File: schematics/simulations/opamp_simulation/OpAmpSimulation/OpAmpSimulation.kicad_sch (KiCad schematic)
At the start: 7 parts, among them U1 ${SIM.PARAMS}

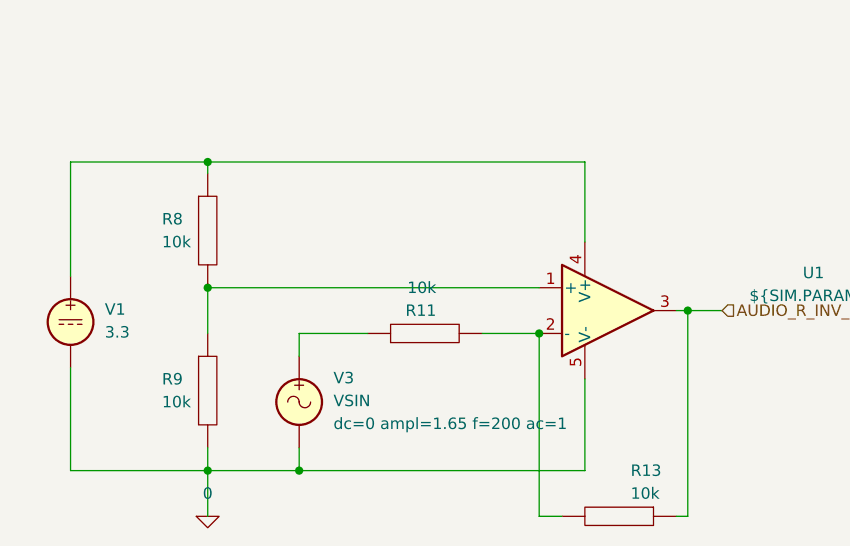
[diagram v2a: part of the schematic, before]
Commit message: [opamp_simulation:OpAmpSimulation] Ref | Replaced "R"s w/ common ones
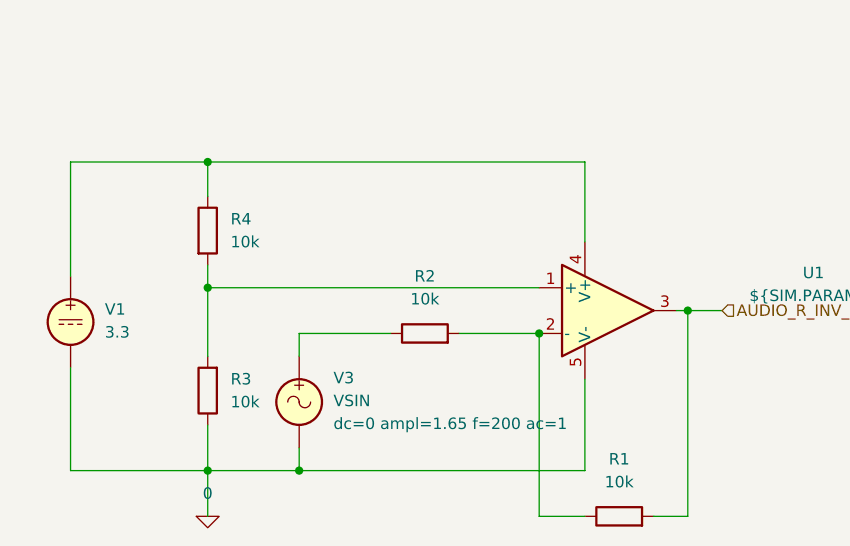
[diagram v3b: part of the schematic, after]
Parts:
- removed R11, R13, R8, R9: 10k, symbol pspice:R
- added R1, R2, R3, R4: 10k, symbol Device:R
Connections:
- net 0: now also R3.1
- net AUDIO_R_INV_SCALED: now also R1.2
- net at U1.4 (V+), V1.1: now also R4.1
- net at V3.1: now also R2.1
- net at U1.2 (-): now also R1.1, R2.2
- net at U1.1 (+): now also R3.2, R4.2
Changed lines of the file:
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@@
     (stroke (width 0) (type default))
   )
-  (wire (pts (xy 58.42 163.83) (xy 58.42 166.37))
+  (wire (pts (xy 107.95 171.45) (xy 111.76 171.45))
     (stroke (width 0) (type default))
   )
@@
     (stroke (width 0) (type default))
   )
-  (wire (pts (xy 58.42 132.08) (xy 58.42 133.35))
+  (wire (pts (xy 58.42 132.08) (xy 58.42 135.89))
     (stroke (width 0) (type default))
   )
@@
     (stroke (width 0) (type default))
   )
-  (wire (pts (xy 88.9 151.13) (xy 95.25 151.13))
-    (stroke (width 0) (type default))
-  )
   (wire (pts (xy 100.33 132.08) (xy 100.33 140.97))
     (stroke (width 0) (type default))
@@
     (stroke (width 0) (type default))
   )
-  (wire (pts (xy 68.58 151.13) (xy 76.2 151.13))
+  (wire (pts (xy 68.58 151.13) (xy 78.74 151.13))
     (stroke (width 0) (type default))
   )
@@
     (stroke (width 0) (type default))
   )
-  (wire (pts (xy 110.49 171.45) (xy 111.76 171.45))
+  (wire (pts (xy 86.36 151.13) (xy 95.25 151.13))
     (stroke (width 0) (type default))
   )
@@
     (stroke (width 0) (type default))
   )
+  (wire (pts (xy 58.42 146.05) (xy 58.42 153.67))
+    (stroke (width 0) (type default))
+  )
   (wire (pts (xy 68.58 166.37) (xy 58.42 166.37))
     (stroke (width 0) (type default))
   )
+  (wire (pts (xy 58.42 161.29) (xy 58.42 166.37))
+    (stroke (width 0) (type default))
+  )
   (wire (pts (xy 43.18 154.94) (xy 43.18 166.37))
     (stroke (width 0) (type default))
   )
-  (wire (pts (xy 58.42 146.05) (xy 58.42 151.13))
+  (wire (pts (xy 58.42 143.51) (xy 58.42 146.05))
     (stroke (width 0) (type default))
   )
@@
     (stroke (width 0) (type default))
   )
-  (wire (pts (xy 97.79 171.45) (xy 95.25 171.45))
+  (wire (pts (xy 95.25 171.45) (xy 100.33 171.45))
     (stroke (width 0) (type default))
   )
@@
     )
   )
-  (symbol (lib_id "pspice:R") (at 82.55 151.13 90) (unit 1)
-    (in_bom yes) (on_board yes) (dnp no)
-    (property "Reference" "R11" (at 83.82 148.59 90)
-      (effects (font (size 1.27 1.27)) (justify left))
-    )
-    (property "Value" "10k" (at 83.82 146.05 90)
-      (effects (font (size 1.27 1.27)) (justify left))
-    )
-    (property "Footprint" "" (at 82.55 151.13 0)
+  (symbol (lib_id "Device:R") (at 82.55 151.13 90) (unit 1)
+    (in_bom yes) (on_board yes) (dnp no) (fields_autoplaced)
+    (property "Reference" "R2" (at 82.55 144.78 90)
+      (effects (font (size 1.27 1.27)))
+    )
+    (property "Value" "10k" (at 82.55 147.32 90)
+      (effects (font (size 1.27 1.27)))
+    )
+    (property "Footprint" "" (at 82.55 152.908 90)
       (effects (font (size 1.27 1.27)) hide)
     )
@@
       (project "OpAmpSimulation"
         (path "/0d0a973c-3ed5-4fec-a6a9-6f11d3a34d9a"
-          (reference "R11") (unit 1)
-        )
-      )
-      (project "stm32f030_adc"
-        (path "/85629656-c73b-4e1f-b8e8-4366f4b01266"
-          (reference "R7") (unit 1)
-        )
-        (path "/85629656-c73b-4e1f-b8e8-4366f4b01266/b4185304-bcce-4cb1-98f3-8bffc8e76c1e"
-          (reference "R15") (unit 1)
-        )
-      )
-    )
-  )
-  (symbol (lib_id "pspice:R") (at 58.42 139.7 0) (unit 1)
-    (in_bom yes) (on_board yes) (dnp no)
-    (property "Reference" "R8" (at 53.34 138.43 0)
-      (effects (font (size 1.27 1.27)) (justify left))
-    )
-    (property "Value" "10k" (at 53.34 140.97 0)
-      (effects (font (size 1.27 1.27)) (justify left))
-    )
-    (property "Footprint" "" (at 58.42 139.7 0)
+          (reference "R2") (unit 1)
+        )
+      )
+    )
+  )
+  (symbol (lib_id "Device:R") (at 58.42 139.7 0) (unit 1)
+    (in_bom yes) (on_board yes) (dnp no) (fields_autoplaced)
+    (property "Reference" "R4" (at 60.96 138.43 0)
+      (effects (font (size 1.27 1.27)) (justify left))
+    )
+    (property "Value" "10k" (at 60.96 140.97 0)
+      (effects (font (size 1.27 1.27)) (justify left))
+    )
+    (property "Footprint" "" (at 56.642 139.7 90)
       (effects (font (size 1.27 1.27)) hide)
     )
@@
       (project "OpAmpSimulation"
         (path "/0d0a973c-3ed5-4fec-a6a9-6f11d3a34d9a"
-          (reference "R8") (unit 1)
-        )
-      )
-      (project "stm32f030_adc"
-        (path "/85629656-c73b-4e1f-b8e8-4366f4b01266"
+          (reference "R4") (unit 1)
+        )
+      )
+    )
+  )
+  (symbol (lib_id "Device:R") (at 58.42 157.48 180) (unit 1)
+    (in_bom yes) (on_board yes) (dnp no) (fields_autoplaced)
+    (property "Reference" "R3" (at 60.96 156.21 0)
+      (effects (font (size 1.27 1.27)) (justify right))
+    )
+    (property "Value" "10k" (at 60.96 158.75 0)
+      (effects (font (size 1.27 1.27)) (justify right))
+    )
+    (property "Footprint" "" (at 60.198 157.48 90)
+      (effects (font (size 1.27 1.27)) hide)
+    )
+    (property "Datasheet" "~" (at 58.42 157.48 0)
+      (effects (font (size 1.27 1.27)) hide)
+    )
+    (pin "1")
+    (pin "2")
+    (instances
+      (project "OpAmpSimulation"
+        (path "/0d0a973c-3ed5-4fec-a6a9-6f11d3a34d9a"
           (reference "R3") (unit 1)
-        )
-        (path "/85629656-c73b-4e1f-b8e8-4366f4b01266/b4185304-bcce-4cb1-98f3-8bffc8e76c1e"
-          (reference "R13") (unit 1)
-        )
-      )
-    )
-  )
-  (symbol (lib_id "pspice:R") (at 104.14 171.45 270) (unit 1)
-    (in_bom yes) (on_board yes) (dnp no)
-    (property "Reference" "R13" (at 105.41 166.37 90)
-      (effects (font (size 1.27 1.27)) (justify left))
-    )
-    (property "Value" "10k" (at 105.41 168.91 90)
-      (effects (font (size 1.27 1.27)) (justify left))
-    )
-    (property "Footprint" "" (at 104.14 171.45 0)
-      (effects (font (size 1.27 1.27)) hide)
-    )
-    (property "Datasheet" "~" (at 104.14 171.45 0)
-      (effects (font (size 1.27 1.27)) hide)
-    )
-    (pin "1")
-    (pin "2")
-    (instances
-      (project "OpAmpSimulation"
-        (path "/0d0a973c-3ed5-4fec-a6a9-6f11d3a34d9a"
-          (reference "R13") (unit 1)
-        )
-      )
-      (project "stm32f030_adc"
-        (path "/85629656-c73b-4e1f-b8e8-4366f4b01266"
-          (reference "R9") (unit 1)
-        )
-        (path "/85629656-c73b-4e1f-b8e8-4366f4b01266/b4185304-bcce-4cb1-98f3-8bffc8e76c1e"
-          (reference "R16") (unit 1)
-        )
-      )
-    )
-  )
-  (symbol (lib_id "pspice:R") (at 58.42 157.48 0) (unit 1)
-    (in_bom yes) (on_board yes) (dnp no)
-    (property "Reference" "R9" (at 53.34 156.21 0)
-      (effects (font (size 1.27 1.27)) (justify left))
-    )
-    (property "Value" "10k" (at 53.34 158.75 0)
-      (effects (font (size 1.27 1.27)) (justify left))
-    )
-    (property "Footprint" "" (at 58.42 157.48 0)
-      (effects (font (size 1.27 1.27)) hide)
-    )
-    (property "Datasheet" "~" (at 58.42 157.48 0)
-      (effects (font (size 1.27 1.27)) hide)
-    )
-    (pin "1")
-    (pin "2")
-    (instances
-      (project "OpAmpSimulation"
-        (path "/0d0a973c-3ed5-4fec-a6a9-6f11d3a34d9a"
-          (reference "R9") (unit 1)
-        )
-      )
-      (project "stm32f030_adc"
-        (path "/85629656-c73b-4e1f-b8e8-4366f4b01266"
-          (reference "R5") (unit 1)
-        )
-        (path "/85629656-c73b-4e1f-b8e8-4366f4b01266/b4185304-bcce-4cb1-98f3-8bffc8e76c1e"
-          (reference "R14") (unit 1)
         )
       )
@@
         )
       )
+    )
+  )
+  (symbol (lib_id "Device:R") (at 104.14 171.45 90) (unit 1)
+    (in_bom yes) (on_board yes) (dnp no) (fields_autoplaced)
+    (property "Reference" "R1" (at 104.14 165.1 90)
+      (effects (font (size 1.27 1.27)))
+    )
+    (property "Value" "10k" (at 104.14 167.64 90)
+      (effects (font (size 1.27 1.27)))
+    )
+    (property "Footprint" "" (at 104.14 173.228 90)
+      (effects (font (size 1.27 1.27)) hide)
+    )
+    (property "Datasheet" "~" (at 104.14 171.45 0)
+      (effects (font (size 1.27 1.27)) hide)
+    )
+    (pin "1")
+    (pin "2")
+    (instances
+      (project "OpAmpSimulation"
+        (path "/0d0a973c-3ed5-4fec-a6a9-6f11d3a34d9a"
+          (reference "R1") (unit 1)
+        )
+      )

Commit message: [opamp_simulation:OpAmpSimulation] Impl | Added various simulations
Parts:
- added C1, C10, C11, C12, C2, C3, C5, C7, C8, C9: 10 uF, symbol Device:C
- added C4, C6: 1 nF, symbol Device:C
- added R10, R13, R14, R15, R16, R18, R19, R20, R21, R22, R23, R5, R6, R7, R8, R9: 10k, symbol Device:R
- added R11, R12: 1k, symbol Device:R
- added R17, R24: 100k, symbol Device:R
- added U2, U3, U4, U5: ${SIM.PARAMS}, symbol Simulation_SPICE:OPAMP
- added V10, V4, V6, V8: VSIN, symbol Simulation_SPICE:VSIN
- added V2, V5, V7: 3.3, symbol Simulation_SPICE:VDC
- R1: value 10k -> 20k
- R2: value 10k -> 5k
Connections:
- net 0: now also C2.1, C4.1, C6.1, C8.1, R10.1, R14.1, R17.1, R19.1, R23.1, R24.1, R6.1, U2.5 (V-), U3.5 (V-), U4.5 (V-), U5.5 (V-), V10.2, V2.2, V4.2, V5.2, V6.2, V7.2, V8.2
- net at R1.1, U1.2 (-): now also C1.2, C2.2; no longer R2.2
- new net: R10.2, R9.1, U3.1 (+)
- new net: C10.2, C3.2, R12.1, U3.2 (-)
- new net: R9.2, U3.4 (V+), V5.1
- new net: C6.2, C7.1, R15.1
- new net: R15.2, V8.1
- new net: R22.1, R23.2, U5.1 (+)
- new net: R18.1, R19.2, R22.2
- new net: R5.2, R6.2, U2.1 (+)
- new net: R13.1, U4.4 (V+), V7.1
- new net: C5.1, R11.1, V6.1
- new net: C10.1, C5.2, R11.2
- new net: C11.2, C12.1, R20.1, R21.2, U5.2 (-)
- new net: C12.2, R20.2, R24.2, U5.3
- new net: C1.1, C4.2, R2.2
- new net: R13.2, R14.2, U4.1 (+)
- new net: R5.1, U2.4 (V+), V2.1
- new net: R7.1, V4.1
- new net: R7.2, R8.1, U2.2 (-)
- new net: C11.1, R21.1, V10.1
- new net: C7.2, C8.2, R16.2, U4.2 (-)
- new net: R16.1, U4.3
- new net: R8.2, U2.3
- new net +3V3: R18.2, U5.4 (V+)
- new net a: C3.1, C9.1, R12.2
- new net b: C9.2, R17.2, U3.3
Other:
- note added: ".tran 0.1 0.05"
- note removed: ".tran 0.1 0.5"
- moved on the sheet: R1, R2

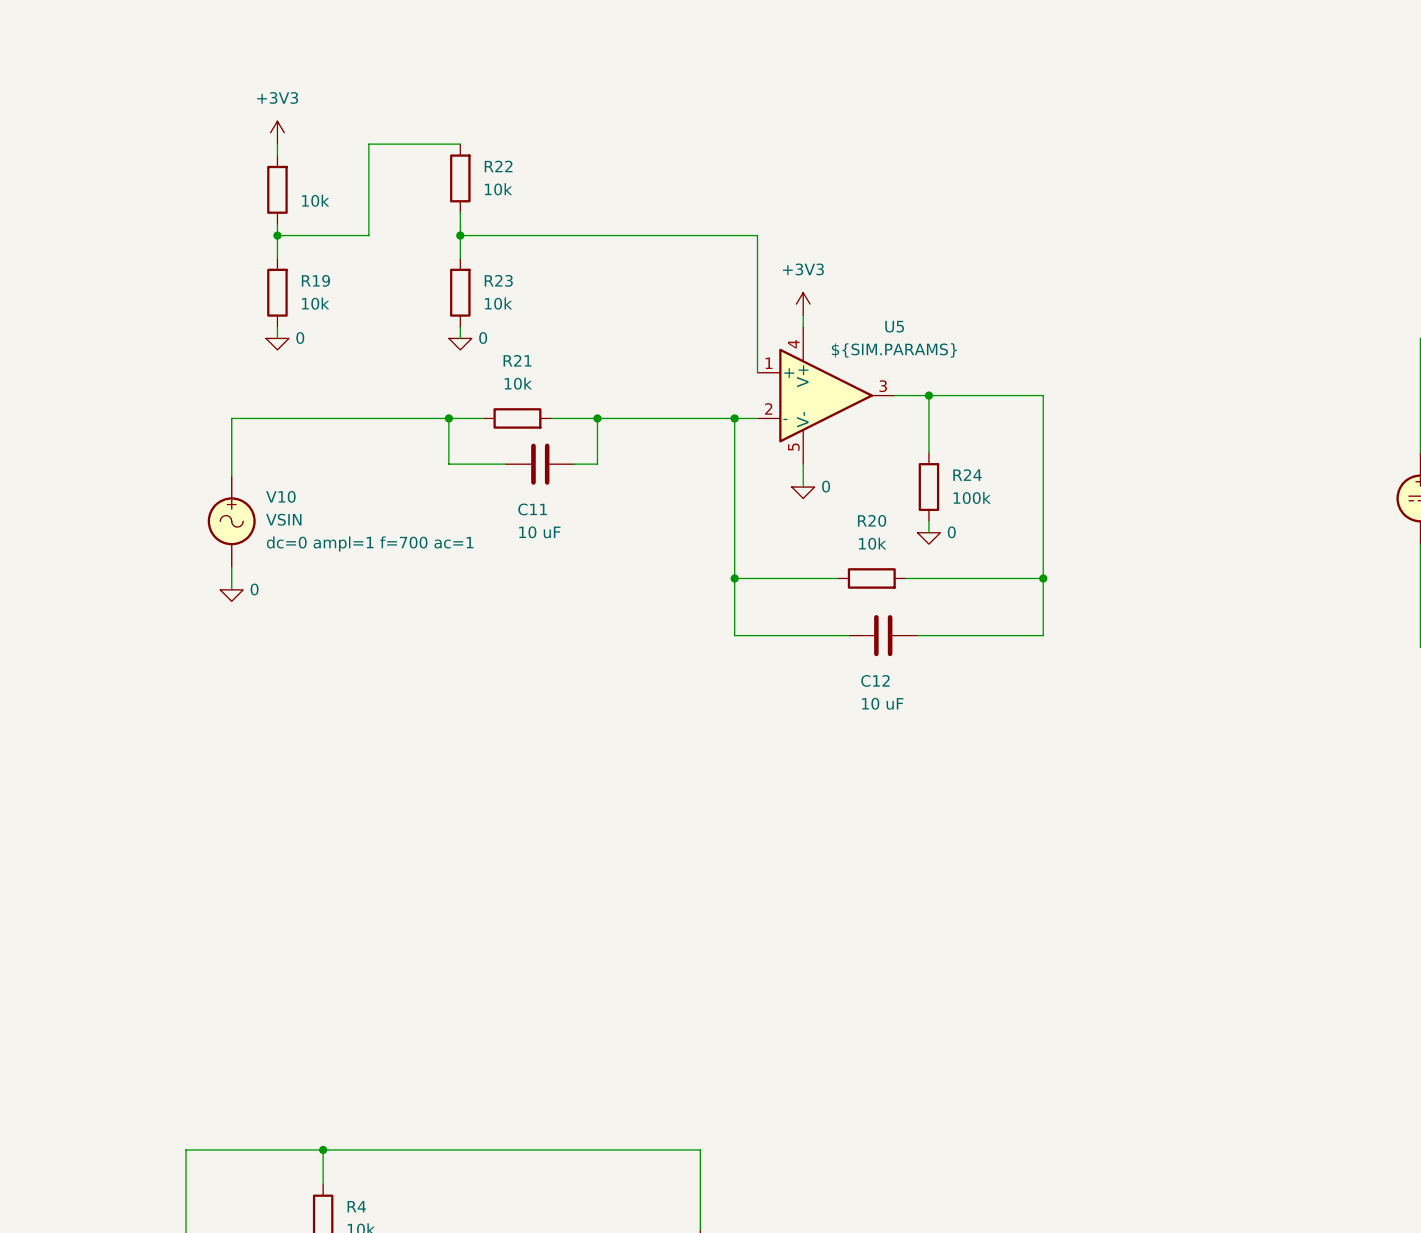
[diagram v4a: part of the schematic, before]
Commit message: [schematics:*] Bug | Fixed OpAmp schematics based on the simulation and practical experiments' results
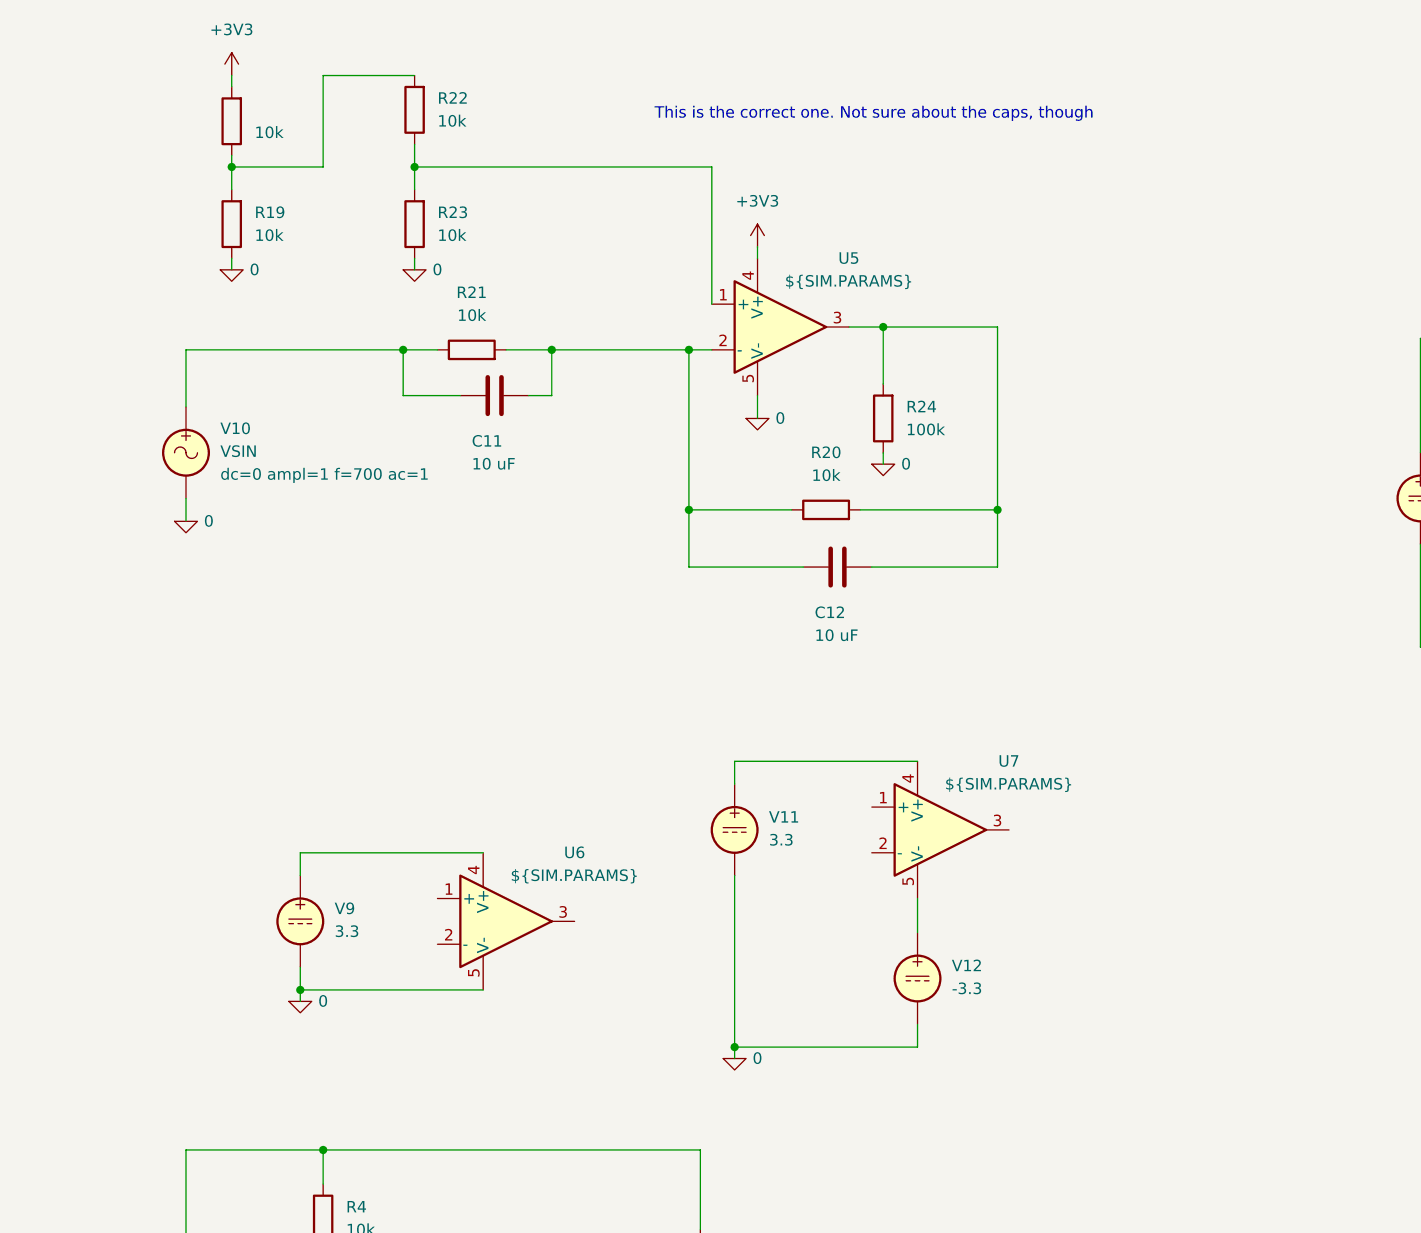
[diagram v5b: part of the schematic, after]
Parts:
- added U6, U7: ${SIM.PARAMS}, symbol Simulation_SPICE:OPAMP
- added V11, V9: 3.3, symbol Simulation_SPICE:VDC
- added V12: -3.3, symbol Simulation_SPICE:VDC
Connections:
- net 0: now also U6.5 (V-), V11.2, V12.2, V9.2
- new net: U7.5 (V-), V12.1
- new net: U6.4 (V+), V9.1
- new net: U7.4 (V+), V11.1
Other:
- note added: "This is the correct one. Not sure about the caps, though"
- moved on the sheet: C11, C12, R19, R20, R21, R22, R23, R24, U5, V10
